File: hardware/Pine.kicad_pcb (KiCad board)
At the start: 2 copper layers, 58.4 x 45.7 mm, 45 parts, among them J1 USB Micro type-B, J2 01x06 Male conn, Q1 p-channel MOSFET, Q2 NPN Transistor, SW1 DIP switch SPST, SW2 Push button, U1 IR Receiver, U2 LDO, U3 Temperature sensor, U4 MCU

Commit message: [design] Enable measuring battery voltage by connecting to GPIO. close #3
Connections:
- R5 pad 2: GND -> /Batt_EN
- U4 pad 25: (no net) -> /Batt_EN
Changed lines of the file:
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@@
     (zones 0)
     (modules 45)
-    (nets 36)
+    (nets 37)
   )
   (page A4)
@@
   (net 34 /SCL)
   (net 35 /IR_Receiver)
+  (net 36 /Batt_EN)
   (net_class Default "This is the default net class."
     (clearance 0.2)
@@
     (add_net /2V8)
     (add_net /Batt)
+    (add_net /Batt_EN)
     (add_net /IR_Emitter)
     (add_net /IR_Receiver)
@@
     (add_net "Net-(Q2-Pad2)")
     (add_net "Net-(R2-Pad1)")
-    (add_net "Net-(U4-Pad1)")
-    (add_net "Net-(U4-Pad10)")
-    (add_net "Net-(U4-Pad13)")
-    (add_net "Net-(U4-Pad14)")
-    (add_net "Net-(U4-Pad15)")
-    (add_net "Net-(U4-Pad16)")
-    (add_net "Net-(U4-Pad19)")
-    (add_net "Net-(U4-Pad2)")
-    (add_net "Net-(U4-Pad20)")
-    (add_net "Net-(U4-Pad21)")
-    (add_net "Net-(U4-Pad22)")
-    (add_net "Net-(U4-Pad23)")
-    (add_net "Net-(U4-Pad25)")
-    (add_net "Net-(U4-Pad27)")
-    (add_net "Net-(U4-Pad28)")
-    (add_net "Net-(U4-Pad29)")
-    (add_net "Net-(U4-Pad3)")
-    (add_net "Net-(U4-Pad30)")
-    (add_net "Net-(U4-Pad37)")
-    (add_net "Net-(U4-Pad38)")
-    (add_net "Net-(U4-Pad4)")
-    (add_net "Net-(U4-Pad41)")
-    (add_net "Net-(U4-Pad47)")
-    (add_net "Net-(U4-Pad7)")
-    (add_net "Net-(U4-Pad8)")
-    (add_net "Net-(U4-Pad9)")
   )
   (module Package_TO_SOT_SMD:SOT-23 (layer F.Cu)
@@
     (pad 26 smd rect (at 4.35 2.25 90) (size 1.3 0.25) (layers F.Cu F.Paste F.Mask)
       (net 32 /LED))
-    (pad 25 smd rect (at 4.35 2.75 90) (size 1.3 0.25) (layers F.Cu F.Paste F.Mask))
+    (pad 25 smd rect (at 4.35 2.75 90) (size 1.3 0.25) (layers F.Cu F.Paste F.Mask)
+      (net 36 /Batt_EN))
     (pad 24 smd rect (at 2.75 4.35 180) (size 1.3 0.25) (layers F.Cu F.Paste F.Mask)
       (net 35 /IR_Receiver))
@@
     (fp_line (start 1 -0.6) (end -0.7 -0.6) (layer F.Fab) (width 0.1))
     (pad 2 smd roundrect (at 1.025 0) (size 1.15 1.4) (layers F.Cu F.Paste F.Mask) (roundrect_rratio 0.217391)
-      (net 2 GND))
+      (net 36 /Batt_EN))
     (pad 1 smd roundrect (at -1.025 0) (size 1.15 1.4) (layers F.Cu F.Paste F.Mask) (roundrect_rratio 0.217391)
       (net 29 /Batt))

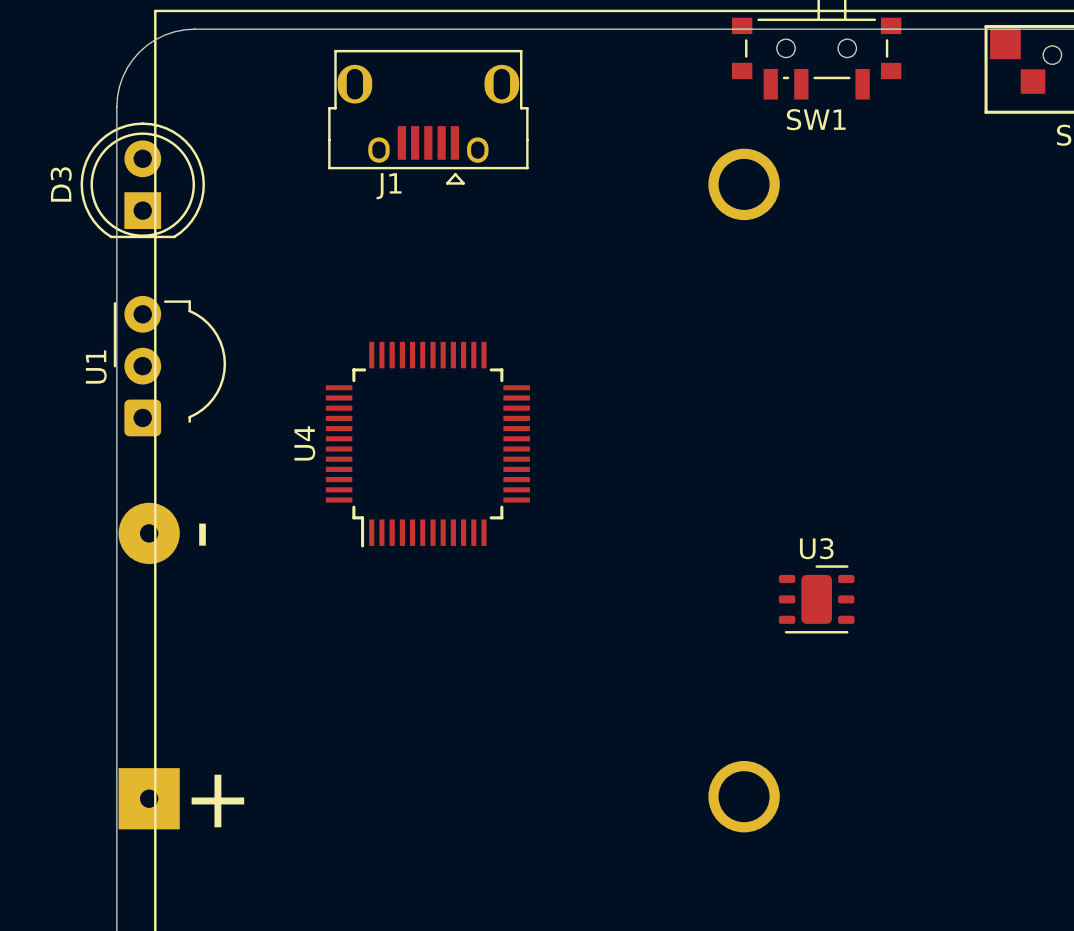
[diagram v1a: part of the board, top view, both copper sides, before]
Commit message: [design] Update BOM with power management circuit tweaks
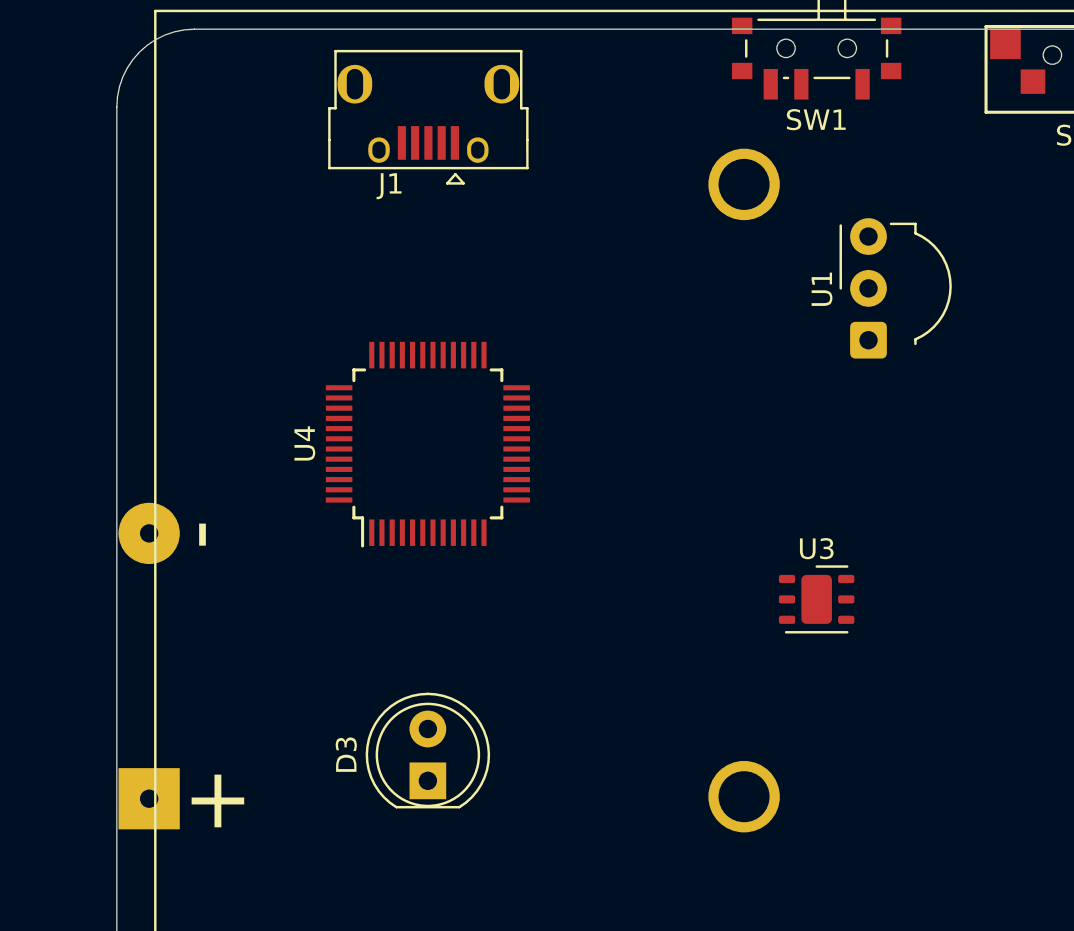
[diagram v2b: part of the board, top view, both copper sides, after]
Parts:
- moved U1 35.8 mm to (139.7, 74.9)
- moved D3 31.2 mm to (118.1, 96.5)
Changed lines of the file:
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@@
   )
   (module OptoDevice:Vishay_MOLD-3Pin (layer F.Cu)
-    (at 104.14 78.74 90)
+    (at 139.7 74.93 90)
     (descr "IR Receiver Vishay TSOP-xxxx, MOLD package, see https://www.vishay.com/docs/82669/tsop32s40f.pdf")
     (tags "IR Receiver Vishay TSOP-xxxx MOLD")
@@
   )
   (module LED_THT:LED_D5.0mm_IRGrey (layer F.Cu)
-    (at 104.14 68.58 90)
+    (at 118.11 96.52 90)
     (descr "LED, diameter 5.0mm, 2 pins, http://cdn-reichelt.de/documents/datenblatt/A500/LL-504BC2E-009.pdf")
     (tags "LED diameter 5.0mm 2 pins")

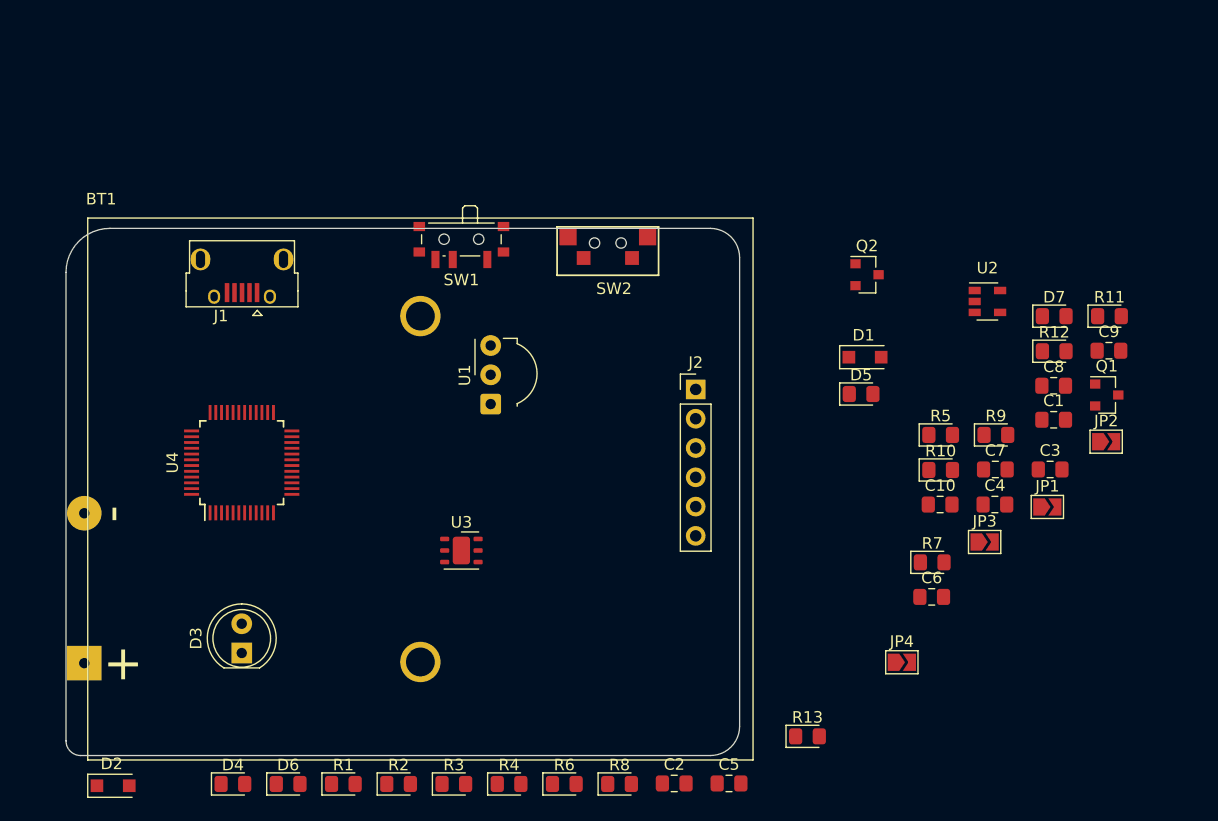
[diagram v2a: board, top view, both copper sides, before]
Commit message: feat: Place components without for mechanical considerations
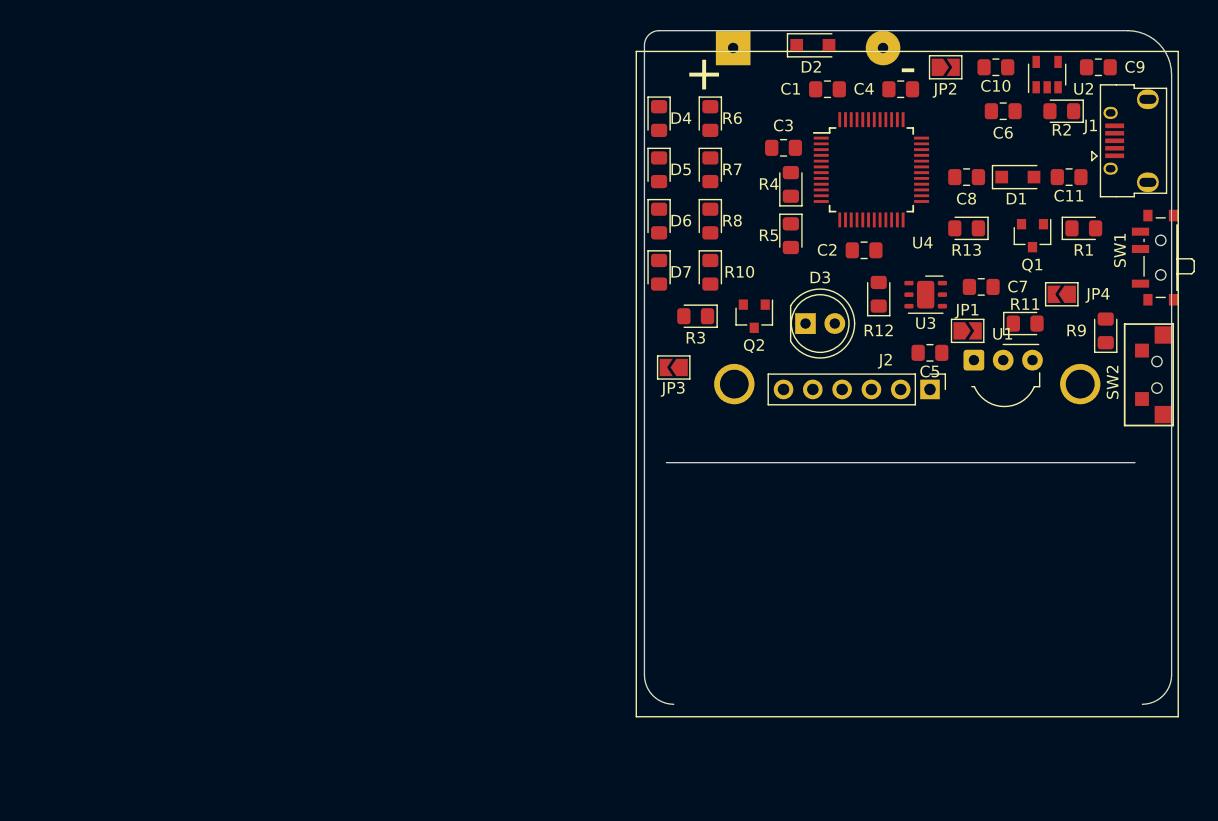
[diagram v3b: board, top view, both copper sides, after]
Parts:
- removed BT1: 3AA batteries: 4.5V, BatteryHolder_Takachi_SN3-3PC_3xAA:BatteryHolder_Takachi_SN3-3PC_3AA
- added C11: 10uF, Capacitor_SMD:C_0805_2012Metric_Pad1.15x1.40mm_HandSolder, F.Cu at (189.9, 55.2)
- added J3: Battery connector, BatteryHolder_Takachi_SN3-3PC_3xAA:BatteryHolder_Takachi_SN3-3PC_3AA, F.Cu at (175.8, 73.2)
- D4, D5, D6, D7: value yellow -> LED Yellow
- SW1: value DIP switch SPST -> Switch
- moved D2 88.4 mm to (167.6, 43.8)
- moved R2 81.9 mm to (189.2, 49.5), turned to 180 degrees
- moved R1 80.3 mm to (191.1, 59.7)
- moved J1 78.3 mm to (195.6, 52.1), turned to 90 degrees
- moved D4 68.5 mm to (154.3, 50.2), turned to 270 degrees
- moved SW1 60.3 mm to (197.5, 62.2), turned to 90 degrees
- moved U4 60.2 mm to (172.7, 54.6), turned to 0 degrees
- moved R6 59.1 mm to (158.8, 50.2), turned to 270 degrees
- moved D6 58.5 mm to (154.3, 59.1), turned to 270 degrees
- moved R4 57.5 mm to (165.7, 55.9), turned to 90 degrees
- moved D3 56.6 mm to (167.0, 67.9), turned to 0 degrees
- moved R8 49.5 mm to (158.8, 59.1), turned to 270 degrees
- moved C2 49.1 mm to (172.1, 61.6)
- moved SW2 49.0 mm to (197.5, 72.4), turned to 270 degrees
- moved R13 46.2 mm to (181.0, 59.7), turned to 180 degrees
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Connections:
- D2 pad 1: Net-(C6-Pad1) -> Net-(D2-Pad1)
- D2 pad 2: Net-(D2-Pad2) -> GND
- Q1 pad 2: Net-(Q1-Pad2) -> Net-(C6-Pad1)
- Q1 pad 3: Net-(D2-Pad2) -> /VBAT
- R4 pad 1: /2V8 -> /VBAT
- SW1 pad 1: Net-(BT1-Pad1) -> Net-(D2-Pad1)
- SW1 pad 2: Net-(Q1-Pad2) -> /VBAT
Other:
- board size 58.4 x 45.7 mm -> 45.7 x 58.4 mm

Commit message: feat: place components mechanically with silkscreen annotations
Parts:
- added REF**: OSHW-Logo2_9.8x8mm_SilkScreen, Symbol:OSHW-Logo2_9.8x8mm_SilkScreen, B.Cu at (175.9, 59.1)
- moved R3 12.5 mm to (169.5, 64.1), turned to 0 degrees
- moved JP3 10.5 mm to (164.4, 77.5)
- moved C5 8.84 mm to (186.1, 67.3)
- moved R11 7.10 mm to (179.7, 71.1), turned to 270 degrees
- moved J2 6.29 mm to (182.2, 78.1)
- moved R10 5.43 mm to (160.7, 68.6), turned to 0 degrees
- moved D7 5.24 mm to (155.6, 68.6), turned to 180 degrees
- moved D3 4.02 mm to (168.3, 71.8), turned to 180 degrees
- moved R8 3.70 mm to (160.7, 62.2), turned to 0 degrees
- moved JP4 3.63 mm to (192.3, 63.5)
- moved Q2 3.59 mm to (165.1, 64.8), turned to 90 degrees
- moved D6 3.42 mm to (155.6, 62.2), turned to 180 degrees
- moved U3 2.54 mm to (177.4, 62.9)
- moved R7 2.29 mm to (160.7, 55.9), turned to 0 degrees
- moved U2 2.29 mm to (189.9, 45.1)
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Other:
- board size 45.7 x 58.4 mm -> 45.7 x 37.5 mm
- board text added: "+"
- board text added: "-"
- board text added: "2.8V"
- board text added: "4.5V"
- board text added: "4.5V 3 AA"
- board text added: "D3"
- board text added: "Get started at hutscape.com/pine"
- board text added: "J1"
- board text added: "LED"
- board text added: "Pine@Hutscape V1.0 2019"
- board text added: "Power LED"
- board text added: "RST"
- board text added: "RX LED"
- board text added: "SW1"
- board text added: "SW2"
- board text added: "SWCLK"
- board text added: "SWDIO"
- board text added: "TX LED"
- board text added: "U1"
- board text added: "dnp"

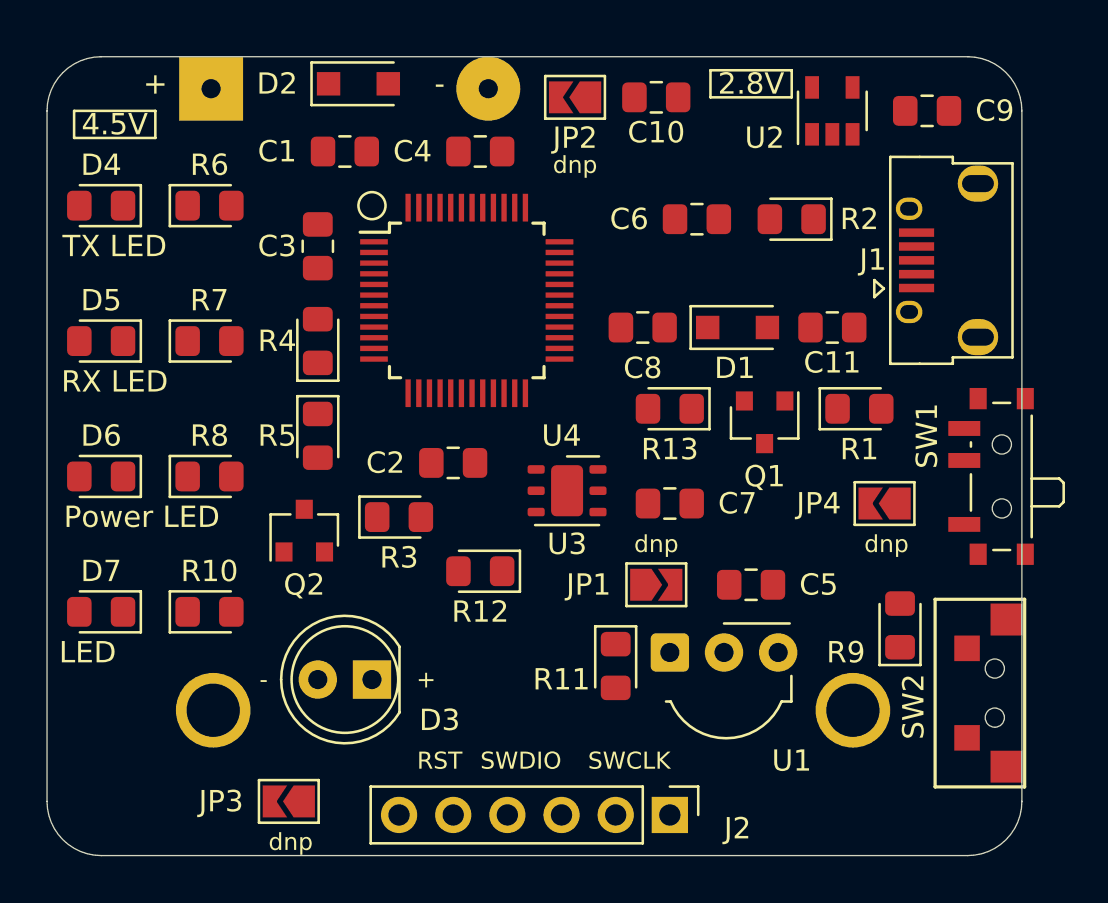
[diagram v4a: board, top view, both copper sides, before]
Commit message: fix: improve components placement. close #9
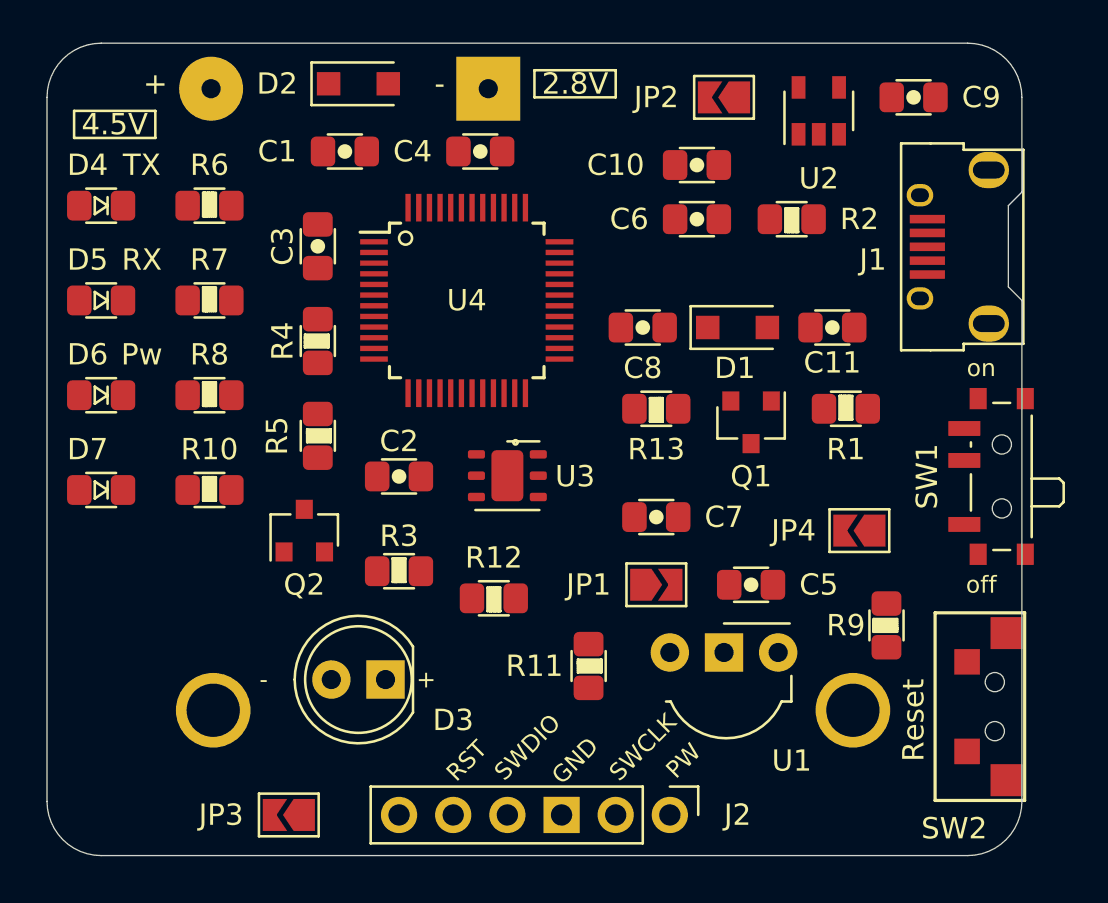
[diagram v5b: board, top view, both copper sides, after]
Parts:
- C1, C10, C11, C2, C3, C4, C5, C6, C7, C8, C9: footprint Capacitor_SMD:C_0805_2012Metric_Pad1.15x1.40mm_HandSolder -> Passives_0805:C_0805_2012Metric_Pad1.15x1.40mm_HandSolder
- D4, D5, D6, D7: footprint LED_SMD:LED_0805_2012Metric_Pad1.15x1.40mm_HandSolder -> Passives_0805:LED_0805_2012Metric_Pad1.15x1.40mm_HandSolder
- R1, R10, R11, R12, R13, R2, R3, R4, R5, R6, R7, R8, R9: footprint LED_SMD:LED_0805_2012Metric_Pad1.15x1.40mm_HandSolder -> Passives_0805:R_0805_2012Metric_Pad1.15x1.40mm_HandSolder
- moved JP2 6.98 mm to (184.8, 44.5)
- moved D7 5.71 mm to (155.6, 62.9)
- moved R10 5.71 mm to (160.7, 62.9)
- moved D6 3.81 mm to (155.6, 58.4)
- moved R8 3.81 mm to (160.7, 58.4)
- moved C10 3.70 mm to (183.5, 47.6)
- moved U3 2.89 mm to (174.6, 62.2)
- moved C2 2.62 mm to (169.5, 62.2)
- moved R3 2.54 mm to (169.5, 66.7)
- moved D5 1.91 mm to (155.6, 54.0)
- moved R7 1.91 mm to (160.7, 54.0)
- moved JP4 1.73 mm to (191.1, 64.8)
- moved R12 1.42 mm to (174.0, 67.9)
- moved R11 1.27 mm to (178.4, 71.1)
- moved C7 0.90 mm to (181.6, 64.1)
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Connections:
- C6 pad 1: Net-(C6-Pad1) -> /SWD_POWER_IN
- D1 pad 1: Net-(C6-Pad1) -> /SWD_POWER_IN
- D4 pad 1: Net-(D4-Pad1) -> (no net)
- D4 pad 2: /2V8 -> (no net)
- D5 pad 1: Net-(D5-Pad1) -> (no net)
- D5 pad 2: /2V8 -> (no net)
- D6 pad 1: Net-(D6-Pad1) -> (no net)
- D6 pad 2: /2V8 -> (no net)
- D7 pad 1: Net-(D7-Pad1) -> (no net)
- D7 pad 2: /2V8 -> (no net)
- J2 pad 1: (no net) -> /SWD_POWER_IN
- Q1 pad 2: Net-(C6-Pad1) -> /SWD_POWER_IN
- R10 pad 1: Net-(D7-Pad1) -> (no net)
- R2 pad 2: Net-(C6-Pad1) -> /SWD_POWER_IN
- R6 pad 1: Net-(D4-Pad1) -> (no net)
- R7 pad 1: Net-(D5-Pad1) -> (no net)
- R8 pad 1: Net-(D6-Pad1) -> (no net)
- U2 pad 1: Net-(C6-Pad1) -> /SWD_POWER_IN
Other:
- board size 45.7 x 37.5 mm -> 45.7 x 38.1 mm
- net class Power added: clearance 0.2, trace_width 0.4, via_dia 0.7, via_drill 0.5
- board text added: "GND"
- board text added: "PW"
- board text added: "Pw"
- board text added: "RX"
- board text added: "Reset"
- board text added: "TX"
- board text added: "off"
- board text added: "on"
- board text removed: "LED"
- board text removed: "Power LED"
- board text removed: "RX LED"
- board text removed: "TX LED"
- board text removed: "dnp"
